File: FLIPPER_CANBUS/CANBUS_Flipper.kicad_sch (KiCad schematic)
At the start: 17 parts, among them J1 Conn_01x10_Socket, J2 Conn_01x08_Socket, J3 Conn_01x02, J4 Conn_01x02_Socket, U1 MCP2515-xST, U2 MAX3051, Y1 16 Mhz

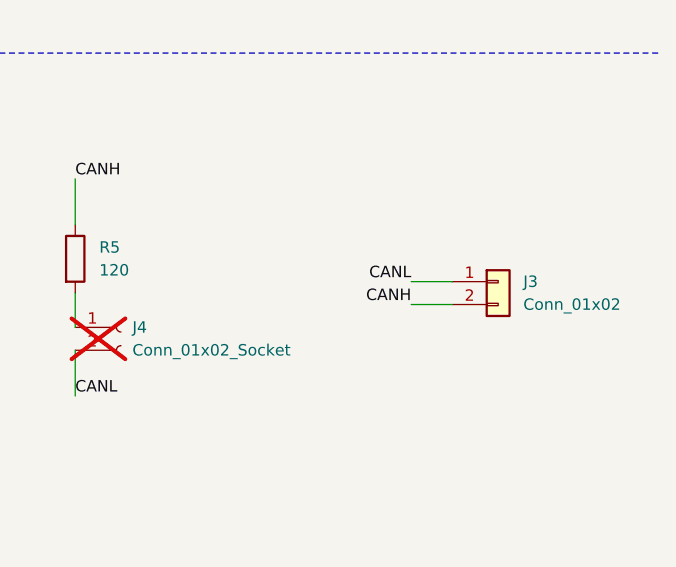
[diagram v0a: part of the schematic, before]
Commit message: fix: orientation of J3 footprint was wrong
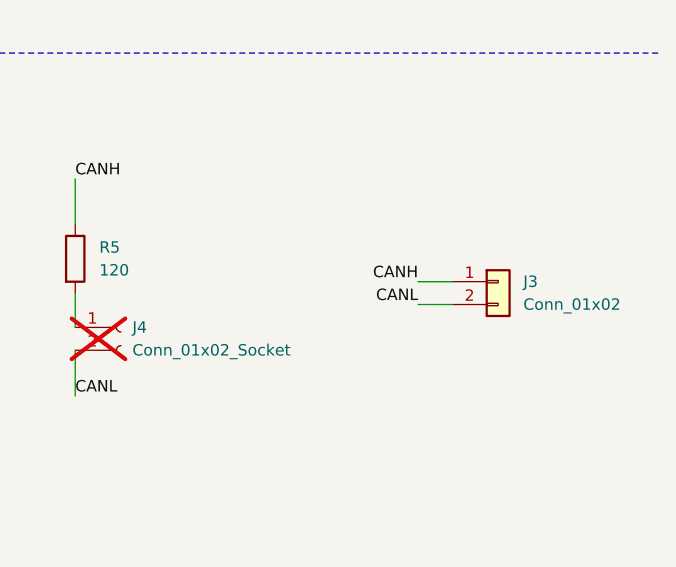
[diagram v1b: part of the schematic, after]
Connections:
- net CANH: now also J3.1 (Pin_1); no longer J3.2 (Pin_2)
- net CANL: now also J3.2 (Pin_2); no longer J3.1 (Pin_1)
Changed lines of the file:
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@@
 	(wire
 		(pts
-			(xy 257.048 127) (xy 261.62 127)
+			(xy 257.81 129.54) (xy 261.62 129.54)
 		)
 		(stroke
@@
 	(wire
 		(pts
+			(xy 257.81 127) (xy 261.62 127)
+		)
+		(stroke
+			(width 0)
+			(type default)
+		)
+	)
+	(wire
+		(pts
 			(xy 43.053 78.359) (xy 46.863 78.359)
 		)
@@
 		(pts
 			(xy 211.455 58.42) (xy 213.487 58.42)
-		)
-		(stroke
-			(width 0)
-			(type default)
-		)
-	)
-	(wire
-		(pts
-			(xy 257.048 129.54) (xy 261.62 129.54)
 		)
 		(stroke
@@
 	)
 	(label "CANH"
-		(at 257.048 129.54 180)
+		(at 257.81 127 180)
 		(fields_autoplaced yes)
 		(effects
@@
 	)
 	(label "CANL"
-		(at 257.048 127 180)
-		(fields_autoplaced yes)
-		(effects
+		(at 257.81 129.54 180)
+		(fields_autoplaced yes)
+		(effects

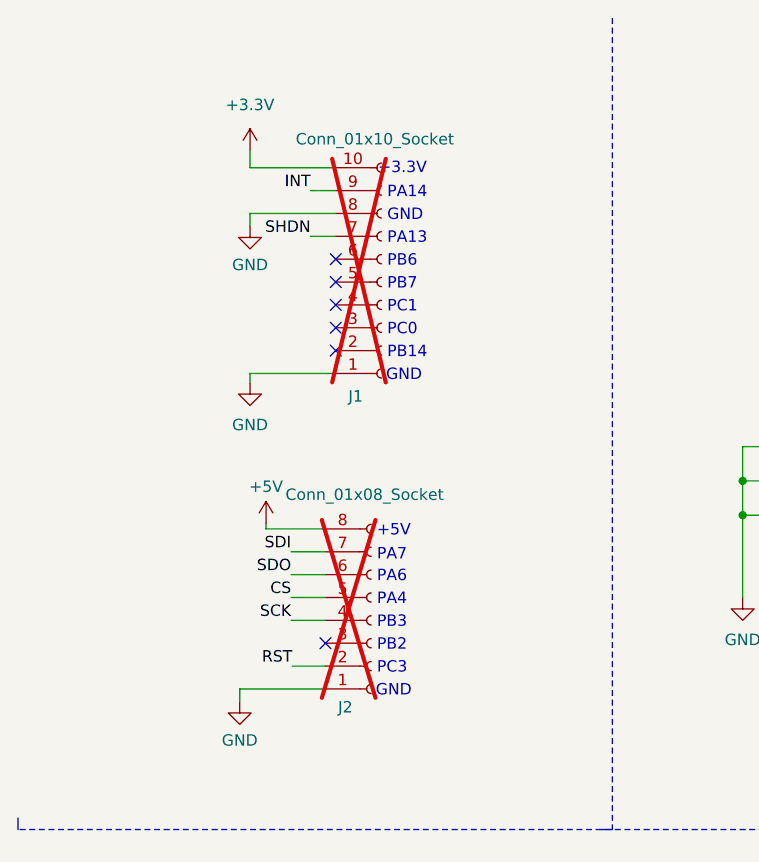
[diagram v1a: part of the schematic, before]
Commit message: feat (hw): remove DNP for J1 and J2
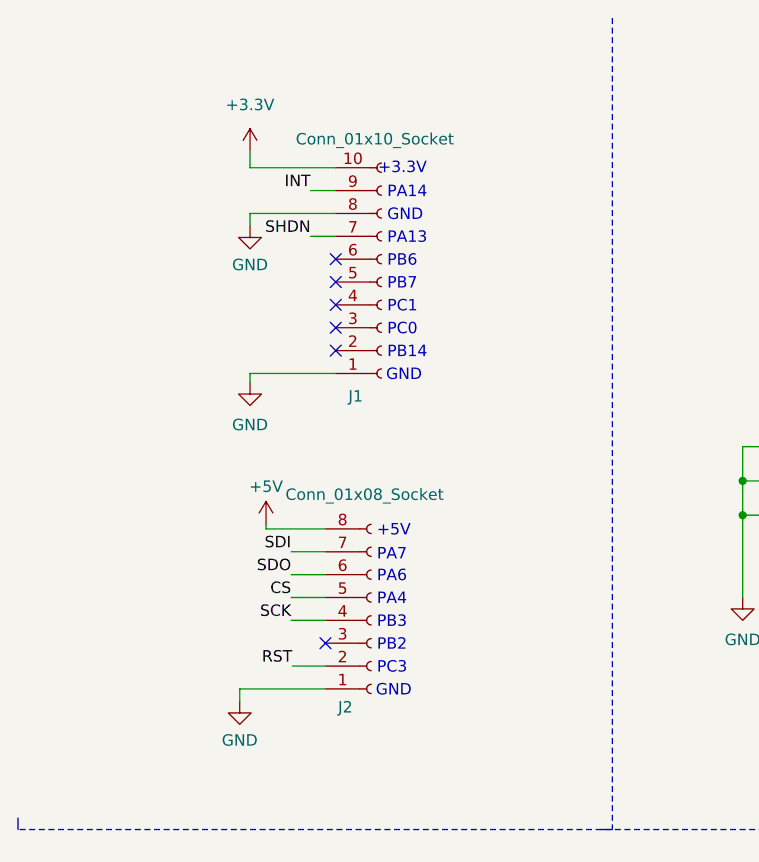
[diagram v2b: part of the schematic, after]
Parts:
- J1, J2: now fitted
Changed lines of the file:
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@@
 		(in_bom yes)
 		(on_board yes)
-		(dnp yes)
+		(dnp no)
 		(property "Reference" "J1"
 			(at 49.403 53.467 0)
@@
 		(in_bom yes)
 		(on_board yes)
-		(dnp yes)
+		(dnp no)
 		(property "Reference" "J2"
 			(at 48.26 88.011 0)

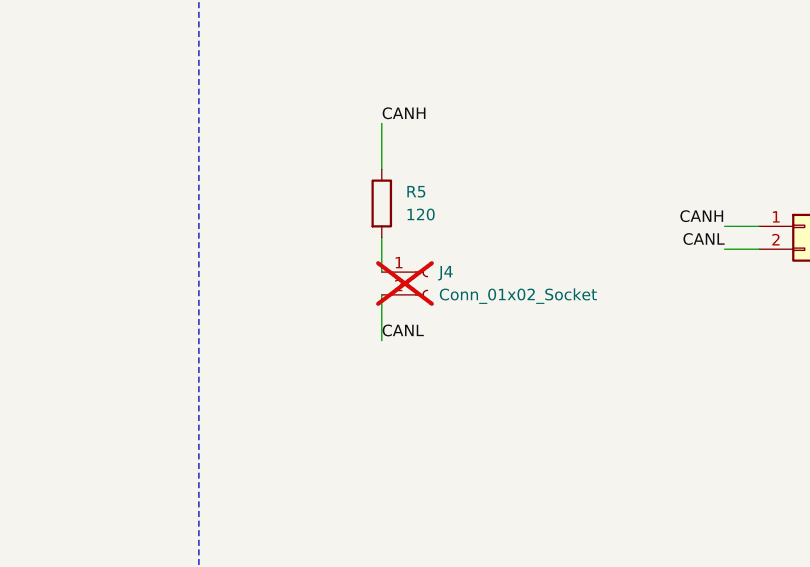
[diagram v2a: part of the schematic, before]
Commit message: fix (hw): remove DNP for J4
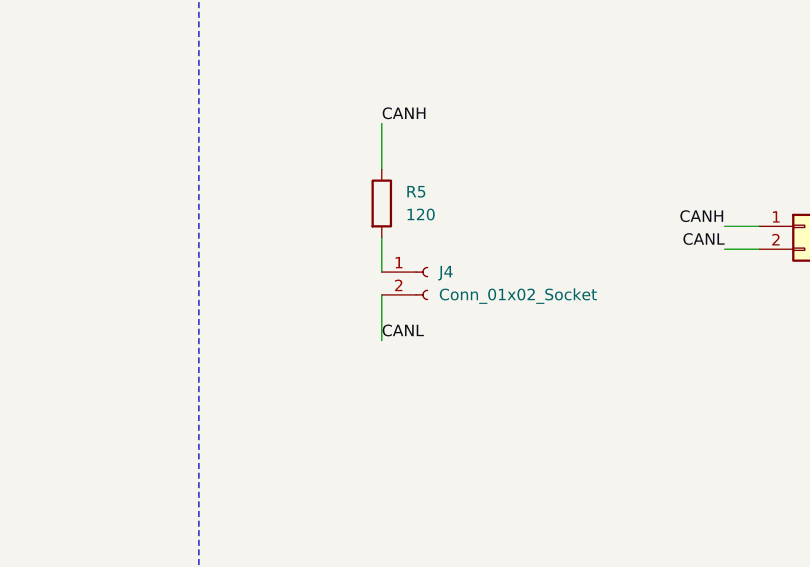
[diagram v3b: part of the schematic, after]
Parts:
- J4: now fitted
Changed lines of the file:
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@@
 		(in_bom yes)
 		(on_board yes)
-		(dnp yes)
+		(dnp no)
 		(fields_autoplaced yes)
 		(property "Reference" "J4"

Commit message: feat(Hw):Update_Schematic
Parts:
- removed J4: Conn_01x02_Socket, Connector_PinHeader_2.54mm:PinHeader_1x02_P2.54mm_Vertical, symbol Connector:Conn_01x02_Socket
- removed R3: 10K, Resistor_SMD:R_0603_1608Metric_Pad0.98x0.95mm_HandSolder, symbol Device:R
- removed R4, R6: 0, Resistor_SMD:R_0603_1608Metric_Pad0.98x0.95mm_HandSolder, symbol Device:R
- removed U1: MCP2515-xST, Package_SO:TSSOP-20_4.4x6.5mm_P0.65mm, symbol Interface_CAN_LIN:MCP2515-xST
- removed U2: MAX3051, Package_TO_SOT_SMD:SOT-23-8_Handsoldering, symbol Interface_UART:MAX3051
- added C5: 0.1uF, Capacitor_SMD:C_0603_1608Metric_Pad1.08x0.95mm_HandSolder, symbol Device:C
- added C6: 4.7nF, Capacitor_SMD:C_0603_1608Metric, symbol Device:C
- added U3: MCP251863T-H-SS, Package_SO:SSOP-28_5.3x10.2mm_P0.65mm, symbol Interface_CAN_LIN:MCP251863T-H-SS
- C2, C3: value 22pF -> 10pF; LCSC# C91701 -> C106245; manf# 0603CG220J500NT -> (none)
- R2: value 10K -> 62; LCSC# C217281 -> C351635; manf# CR-03JL7---10K -> (none)
- R5: value 120 -> 62; LCSC# C2828631 -> C351635; manf# AR03BTCX1200 -> (none)
- Y1: value 16 Mhz -> 40MHz
- renumbered J2 to J1, J1 to J2
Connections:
- net +3.3V: now also U3.1 (VIO), U3.14 (VDD); no longer R2.2
- net +5V: now also C5.1, U3.25 (VCC)
- net CANH: now also R2.1, U3.4 (CANH); no longer R5.1
- net CANL: now also R5.2, U3.3 (CANL)
- net CS: now also U3.13 (~{CS})
- net GND: now also C5.2, C6.2, U3.22 (VSS), U3.24 (GND)
- net INT: now also U3.19 (~{INT}); no longer R2.1
- net SCK: now also U3.9 (SCK)
- net SDI: now also U3.10 (SDI)
- net SDO: now also U3.11 (SDO)
- net at C2.2, Y1.1: now also U3.20 (OSC2)
- net at C3.2, Y1.3: now also U3.21 (OSC1)
- net INT1: now reaches J2.3 (Pin_3)
- net INT1: now also U3.6 (~{INT1})
- net INT0: now reaches J2.5 (Pin_5)
- net INT0: now also U3.7 (~{INT0})
- net RST renamed STBY
- net STBY: now also U3.5 (STBY)
- net SHDN: no longer names the net of J2.7 (Pin_7)
- new net: U3.15 (TXCAN), U3.23 (TXD)
- new net: U3.16 (RXCAN), U3.28 (RXD)
- new net: C6.1, R2.2, R5.1
- no-connect marks 12 -> 6
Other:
- moved on the sheet: C1, C2, C3, J2, J3, R1, R5, Y1

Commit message: feat(Hw):Update_Schematic
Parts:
- added C10, C9: 10uF, Capacitor_SMD:C_0603_1608Metric, symbol Device:C
- added C11: 0.1uF, Capacitor_SMD:C_0603_1608Metric_Pad1.08x0.95mm_HandSolder, symbol Device:C
- added C7, C8: 47pF, Capacitor_SMD:C_0603_1608Metric, symbol Device:C
- added D1, D2: MMBZ27VCL-7-F, Package_TO_SOT_SMD:SOT-23, symbol Diode:MMBZxx
- added JP1: STBY SEL, symbol Jumper:Jumper_3_Open
- added JP2: STBY, symbol Jumper:Jumper_3_Open
- C1: value 0.1uF -> 10uF; footprint Capacitor_SMD:C_0603_1608Metric_Pad1.08x0.95mm_HandSolder -> Capacitor_SMD:C_0603_1608Metric; LCSC# C14663 -> C19702; Manufactura LCSC -> (none); manf# CC0603KRX7R9BB104 -> (none)
- C4, C5: manf# CC0603KRX7R9BB104 -> (none)
- J1: manf# PH2.54-01-08PZD -> (none)
- J2: manf# DS1021-1x10SF11-B -> (none)
- J3: value Conn_01x02 -> Conn; manf# TRT-02 -> (none)
- R1: manf# CR-03JL7---10K -> (none)
- R2, R5: value 62 -> 60; LCSC# C351635 -> C166918
- U3: LCSC# (none) -> C5226885
- Y1: LCSC# C254270 -> (none); manf# X2C016000B91H-R -> (none)
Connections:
- net +3.3V: now also C5.2, C10.2
- net +5V: now also C11.2, C9.2; no longer C5.1
- net CANH: now also C7.2, D1.1 (K)
- net CANL: now also C8.1, D2.2 (K)
- net GND: now also C5.1, C10.1, C11.1, C7.1, C8.2, C9.1, D1.2 (K), D2.1 (K), JP2.1 (A); no longer C5.2
- net INT0: now also JP1.1 (A)
- net STBY: now also JP1.3 (B); no longer U3.5 (STBY)
- new net: JP1.2 (C), JP2.3 (B)
- new net STB: JP2.2 (C), U3.5 (STBY)
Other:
- moved on the sheet: C2, C3, C4, C6, J1, J2, J3, R1, R2, R5, U3, Y1

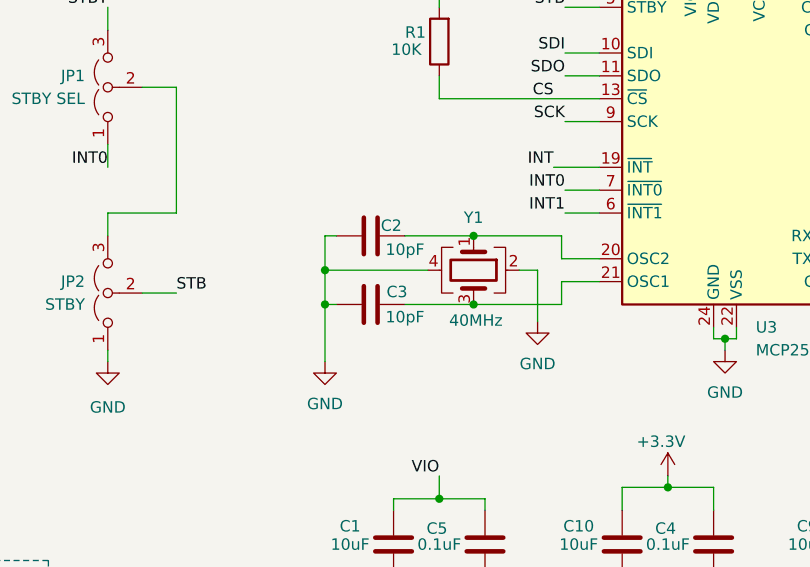
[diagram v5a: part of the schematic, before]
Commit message: feat(Hw):Update_Schematic_And_Init_Route
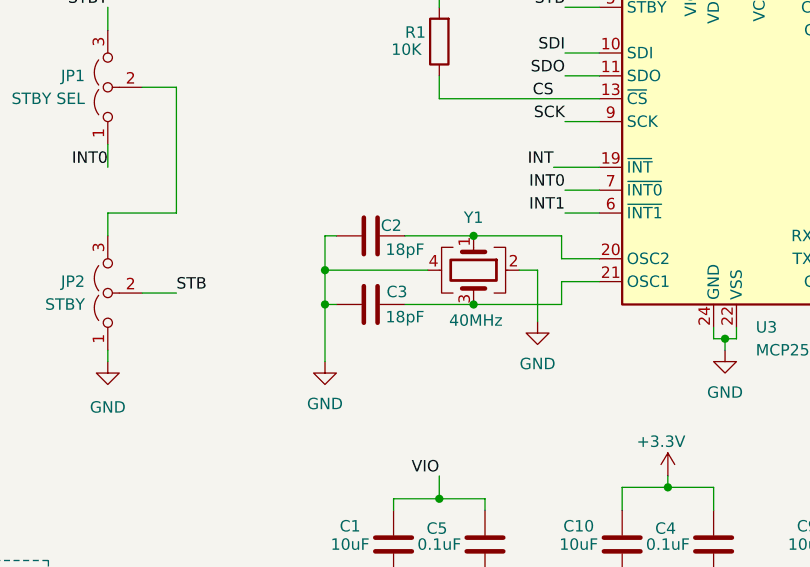
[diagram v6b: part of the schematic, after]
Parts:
- C11, C4, C5: footprint Capacitor_SMD:C_0603_1608Metric_Pad1.08x0.95mm_HandSolder -> Capacitor_SMD:C_0603_1608Metric
- C2, C3: value 10pF -> 18pF; footprint Capacitor_SMD:C_0603_1608Metric_Pad1.08x0.95mm_HandSolder -> Capacitor_SMD:C_0603_1608Metric; LCSC# C106245 -> C5137620
- JP1, JP2: footprint (none) -> Footprints:Jumper
- R1, R2, R5: footprint Resistor_SMD:R_0603_1608Metric_Pad0.98x0.95mm_HandSolder -> Resistor_SMD:R_0603_1608Metric
- Y1: footprint Crystal:Crystal_SMD_2016-4Pin_2.0x1.6mm -> Crystal:Crystal_SMD_EuroQuartz_MT-4Pin_3.2x2.5mm; LCSC# (none) -> C1985459
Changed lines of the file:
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@@
 			)
 		)
-		(property "Footprint" "Capacitor_SMD:C_0603_1608Metric_Pad1.08x0.95mm_HandSolder"
+		(property "Footprint" "Capacitor_SMD:C_0603_1608Metric"
 			(at 162.8648 86.36 0)
 			(effects
@@
 			)
 		)
-		(property "Footprint" "Capacitor_SMD:C_0603_1608Metric_Pad1.08x0.95mm_HandSolder"
+		(property "Footprint" "Capacitor_SMD:C_0603_1608Metric"
 			(at 137.4648 86.36 0)
 			(effects
@@
 			)
 		)
-		(property "Footprint" "Resistor_SMD:R_0603_1608Metric_Pad0.98x0.95mm_HandSolder"
+		(property "Footprint" "Resistor_SMD:R_0603_1608Metric"
 			(at 135.128 34.29 90)
 			(effects
@@
 			)
 		)
-		(property "Value" "10pF"
+		(property "Value" "18pF"
 			(at 129.54 57.404 90)
 			(effects
@@
 			)
 		)
-		(property "Footprint" "Capacitor_SMD:C_0603_1608Metric_Pad1.08x0.95mm_HandSolder"
+		(property "Footprint" "Capacitor_SMD:C_0603_1608Metric"
 			(at 129.54 54.9148 0)
 			(effects
@@
 			)
 		)
-		(property "LCSC#" "C106245"
+		(property "LCSC#" "C5137620"
 			(at 125.73 55.88 0)
 			(effects
@@
 			)
 		)
-		(property "Value" "10pF"
+		(property "Value" "18pF"
 			(at 129.54 64.897 90)
 			(effects
@@
 			)
 		)
-		(property "Footprint" "Capacitor_SMD:C_0603_1608Metric_Pad1.08x0.95mm_HandSolder"
+		(property "Footprint" "Capacitor_SMD:C_0603_1608Metric"
 			(at 129.54 62.5348 0)
 			(effects
@@
 			)
 		)
-		(property "LCSC#" "C106245"
+		(property "LCSC#" "C5137620"
 			(at 125.73 63.5 0)
 			(effects
@@
 			)
 		)
-		(property "Footprint" "Capacitor_SMD:C_0603_1608Metric_Pad1.08x0.95mm_HandSolder"
+		(property "Footprint" "Capacitor_SMD:C_0603_1608Metric"
 			(at 188.2648 86.36 0)
 			(effects
@@
 			)
 		)
-		(property "Footprint" "Resistor_SMD:R_0603_1608Metric_Pad0.98x0.95mm_HandSolder"
+		(property "Footprint" "Resistor_SMD:R_0603_1608Metric"
 			(at 22.352 119.38 90)
 			(effects
@@
 			)
 		)
-		(property "Footprint" "Crystal:Crystal_SMD_2016-4Pin_2.0x1.6mm"
+		(property "Footprint" "Crystal:Crystal_SMD_EuroQuartz_MT-4Pin_3.2x2.5mm"
 			(at 137.16 59.69 0)
 			(effects
@@
 			)
 		)
-		(property "LCSC#" ""
+		(property "LCSC#" "C1985459"
 			(at 137.16 59.69 0)
 			(effects
@@
 			)
 		)
-		(property "Footprint" ""
+		(property "Footprint" "Footprints:Jumper"
 			(at 96.52 39.37 0)
 			(effects
@@
 			)
 		)
-		(property "Footprint" "Resistor_SMD:R_0603_1608Metric_Pad0.98x0.95mm_HandSolder"
+		(property "Footprint" "Resistor_SMD:R_0603_1608Metric"
 			(at 22.352 109.22 90)
 			(effects
@@
 			)
 		)
-		(property "Footprint" ""
+		(property "Footprint" "Footprints:Jumper"
 			(at 96.52 62.23 0)
 			(effects

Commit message: feat(Hw):Update_Route
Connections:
- net CANH renamed CAN+
- net CANL renamed CAN-
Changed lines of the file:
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@@
 		)
 	)
-	(label "CANH"
+	(label "CAN+"
 		(at 21.59 102.87 180)
 		(effects
@@
 		)
 	)
-	(label "CANH"
+	(label "CAN+"
 		(at 185.42 30.48 0)
 		(effects
@@
 		)
 	)
-	(label "CANL"
+	(label "CAN-"
 		(at 21.59 125.73 180)
 		(effects
@@
 		)
 	)
-	(label "CANL"
+	(label "CAN-"
 		(at 185.42 33.02 0)
 		(effects

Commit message: feat(Hw):Update_Schematic_And_Route
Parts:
- R2, R5: value 60 -> 60.2; LCSC# C166918 -> C2086358
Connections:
- net CLK0: now reaches U3.18 (CLKO)
- net CLK0: now also J2.4 (Pin_4)
- no-connect marks 6 -> 4
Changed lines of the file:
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@@
 	)
 	(no_connect
-		(at 181.61 60.96)
-	)
-	(no_connect
 		(at 46.99 33.02)
 	)
@@
 		(at 46.99 43.18)
 	)
-	(no_connect
-		(at 46.99 38.1)
-	)
 	(wire
 		(pts
@@
 	(wire
 		(pts
+			(xy 184.15 60.96) (xy 181.61 60.96)
+		)
+		(stroke
+			(width 0)
+			(type default)
+		)
+	)
+	(wire
+		(pts
 			(xy 133.35 85.09) (xy 138.43 85.09)
 		)
@@
 	(wire
 		(pts
+			(xy 44.45 38.1) (xy 46.99 38.1)
+		)
+		(stroke
+			(width 0)
+			(type default)
+		)
+	)
+	(wire
+		(pts
 			(xy 43.18 71.12) (xy 46.99 71.12)
 		)
@@
 		)
 	)
+	(label "CLK0"
+		(at 44.45 38.1 180)
+		(effects
+			(font
+				(size 1.27 1.27)
+			)
+			(justify right bottom)
+		)
+	)
 	(label "SDO"
 		(at 43.18 66.04 180)
@@
 		)
 	)
+	(label "CLK0"
+		(at 184.15 60.96 0)
+		(effects
+			(font
+				(size 1.27 1.27)
+			)
+			(justify left bottom)
+		)
+	)
 	(label "CAN-"
 		(at 185.42 33.02 0)
@@
 			)
 		)
-		(property "Value" "60"
+		(property "Value" "60.2"
 			(at 20.066 120.396 0)
 			(effects
@@
 			)
 		)
-		(property "LCSC#" "C166918"
+		(property "LCSC#" "C2086358"
 			(at 24.13 119.38 0)
 			(effects
@@
 			)
 		)
-		(property "Value" "60"
+		(property "Value" "60.2"
 			(at 20.066 110.236 0)
 			(effects
@@
 			)
 		)
-		(property "LCSC#" "C166918"
+		(property "LCSC#" "C2086358"
 			(at 24.13 109.22 0)
 			(effects
